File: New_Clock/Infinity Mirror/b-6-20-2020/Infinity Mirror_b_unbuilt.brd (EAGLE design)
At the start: 81 x 26 mm, 19 parts, among them IC1 MSGEQ7P, J1 Vsupply, J2 AUDIO_POTS, J3 LED, U1 DS1307, Y1 32.768kHz

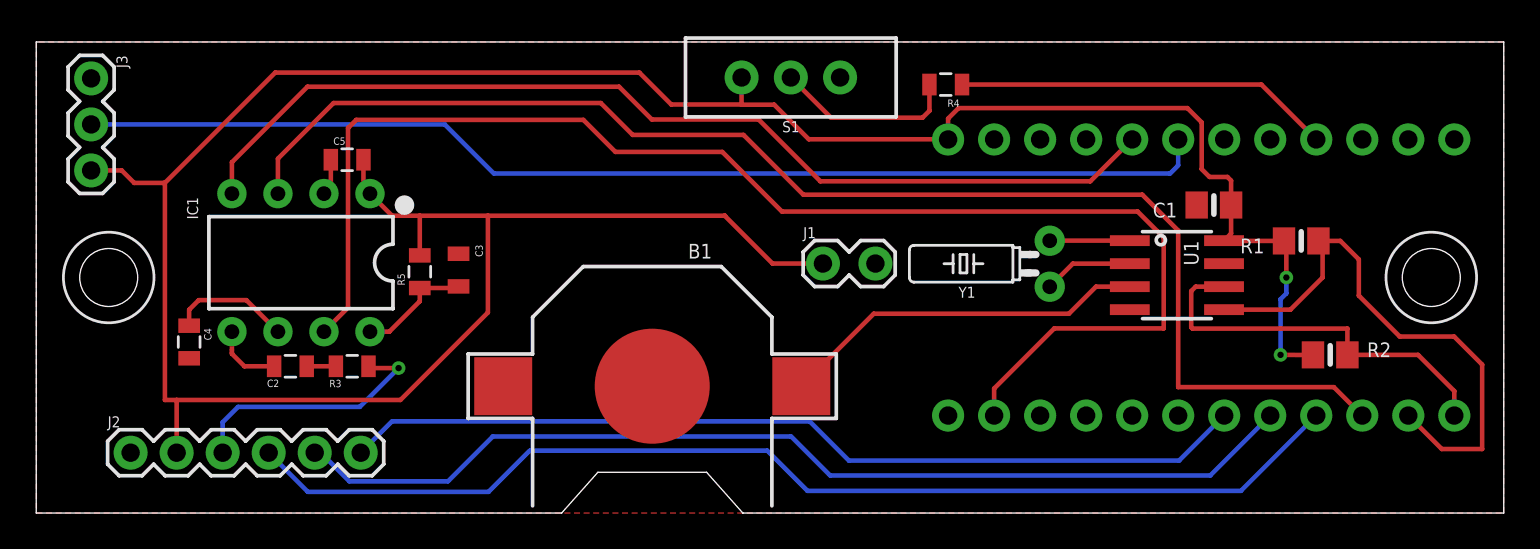
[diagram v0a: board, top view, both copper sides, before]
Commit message: created rec v with a larger board with integrated 8 throw switches. found 3D models and ported circuit box for editing in Fusion. NOTE: THIS CAD IS NOT EXACTLY THE SAME AS THE REAL CLOCK
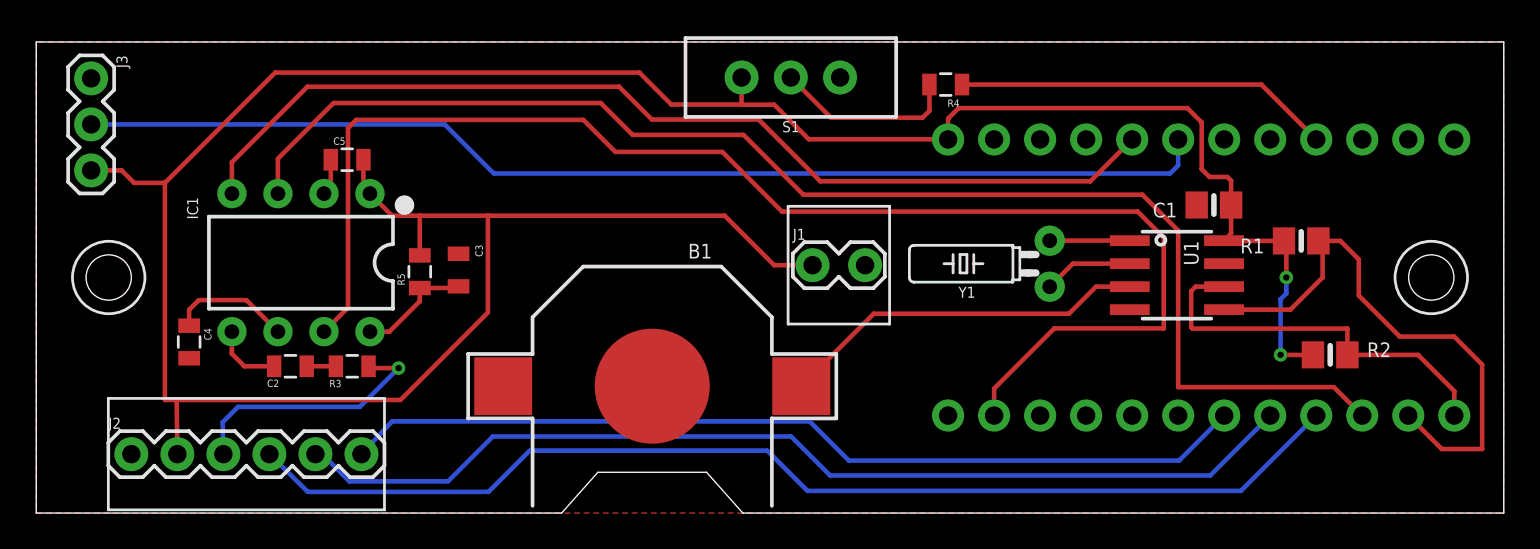
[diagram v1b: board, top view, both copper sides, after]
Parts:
- moved J1 0.58 mm to (43.0, 13.7)
- moved J2 0.09 mm to (5.25, 3.25)
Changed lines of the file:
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@@
 <wire x1="81" y1="26" x2="0" y2="26" width="0" layer="20"/>
 <wire x1="0" y1="26" x2="0" y2="0" width="0" layer="20"/>
-<hole x="77" y="13" drill="3.2"/>
-<circle x="77" y="13" radius="2.5" width="0.1524" layer="21"/>
-<hole x="4" y="13" drill="3.2"/>
-<circle x="4" y="13" radius="2.5" width="0.1524" layer="21"/>
+<hole x="77" y="13" drill="2.5"/>
+<circle x="77" y="13" radius="2" width="0.1524" layer="21"/>
+<hole x="4" y="13" drill="2.5"/>
+<circle x="4" y="13" radius="2" width="0.1524" layer="21"/>
 <wire x1="0" y1="0" x2="29" y2="0" width="0" layer="20"/>
 <wire x1="29" y1="0" x2="31" y2="2.25" width="0" layer="20"/>
@@
 <wire x1="37" y1="2.25" x2="39" y2="0" width="0" layer="20"/>
 <wire x1="39" y1="0" x2="81" y2="0" width="0" layer="20"/>
+<wire x1="3.98" y1="0.175" x2="3.98" y2="6.325" width="0.1524" layer="21"/>
+<wire x1="3.98" y1="6.325" x2="19.22" y2="6.325" width="0.1524" layer="21"/>
+<wire x1="19.22" y1="6.325" x2="19.22" y2="0.175" width="0.1524" layer="21"/>
+<wire x1="19.22" y1="0.175" x2="3.98" y2="0.175" width="0.1524" layer="21"/>
 </plain>
 <attributes>
@@
 </autorouter>
 <elements>
-<element name="J1" library="RC1a_Main_2-20-2018_m" package="SPARKFUN-CONNECTORS_1X02_LOCK" value="Vsupply" x="43.6" y="13.77" smashed="yes">
-<attribute name="NAME" x="42.33" y="15.167" size="0.6096" layer="25" font="vector" ratio="20"/>
-<attribute name="VALUE" x="42.33" y="11.738" size="0.6096" layer="27" font="vector" ratio="20"/>
+<element name="J1" library="RC1a_Main_2-20-2018_m" package="SPARKFUN-CONNECTORS_1X02_LOCK" value="Vsupply" x="43.03" y="13.68" smashed="yes">
+<attribute name="NAME" x="41.76" y="15.077" size="0.6096" layer="25" font="vector" ratio="20"/>
+<attribute name="VALUE" x="41.76" y="11.648" size="0.6096" layer="27" font="vector" ratio="20"/>
 </element>
 <element name="R2" library="microbuilder" package="0805-NO" value="10K" x="71.42" y="8.73" smashed="yes">
@@
 <attribute name="VALUE" x="13.724" y="6.953" size="0.4064" layer="27"/>
 </element>
-<element name="J2" library="SparkFun-Connectors" library_urn="urn:adsk.eagle:library:513" package="1X06" package3d_urn="urn:adsk.eagle:package:38009/1" value="AUDIO_POTS" x="5.21" y="3.33" smashed="yes">
-<attribute name="NAME" x="3.94" y="4.727" size="0.6096" layer="25" font="vector" ratio="20"/>
-<attribute name="PROD_ID" value="CONN-08437" x="5.21" y="3.33" size="1.778" layer="27" display="off"/>
-<attribute name="VALUE" x="3.94" y="1.298" size="0.6096" layer="27" font="vector" ratio="20"/>
+<element name="J2" library="SparkFun-Connectors" library_urn="urn:adsk.eagle:library:513" package="1X06" package3d_urn="urn:adsk.eagle:package:38009/1" value="AUDIO_POTS" x="5.25" y="3.25" smashed="yes">
+<attribute name="NAME" x="3.98" y="4.647" size="0.6096" layer="25" font="vector" ratio="20"/>
+<attribute name="PROD_ID" value="CONN-08437" x="5.25" y="3.25" size="1.778" layer="27" display="off"/>
+<attribute name="VALUE" x="3.98" y="1.218" size="0.6096" layer="27" font="vector" ratio="20"/>
 </element>
 <element name="R5" library="RC1a_Main_2-20-2018_m" package="SPARKFUN-PASSIVES_0805" value="200k" x="21.17" y="13.32" smashed="yes" rot="R90">
@@
 <contactref element="U$1" pad="TG"/>
 <contactref element="S1" pad="3"/>
-<wire x1="3.0378" y1="23.9978" x2="3.03" y2="23.99" width="0.1524" layer="1"/>
 <contactref element="IC1" pad="2"/>
 <polygon width="0.127" layer="1">
@@
 <contactref element="J3" pad="3"/>
 <wire x1="7.1022" y1="18.14" x2="7.1022" y2="6.24" width="0.254" layer="1"/>
-<wire x1="7.75" y1="6.24" x2="7.75" y2="3.33" width="0.254" layer="1"/>
+<wire x1="7.75" y1="6.24" x2="7.79" y2="3.25" width="0.254" layer="1"/>
 <wire x1="64.3276" y1="21.56" x2="64.3276" y2="18.98" width="0.254" layer="1"/>
 <wire x1="64.3276" y1="18.98" x2="64.7576" y2="18.55" width="0.254" layer="1"/>
@@
 <contactref element="IC1" pad="1"/>
 <contactref element="C5" pad="2"/>
-<wire x1="18.06" y1="19.5" x2="18.06" y2="17.99" width="0.254" layer="1"/>
+<wire x1="18.06" y1="17.99" x2="18.06" y2="19.5" width="0.254" layer="1"/>
 <wire x1="18.42" y1="17.63" x2="19.64" y2="16.41" width="0.254" layer="1"/>
 <wire x1="24.93" y1="11.0667125" x2="20.1032875" y2="6.24" width="0.254" layer="1"/>
 <wire x1="24.93" y1="16.41" x2="38" y2="16.41" width="0.254" layer="1"/>
-<wire x1="38" y1="16.41" x2="38.02" y2="16.41" width="0.254" layer="1"/>
 <wire x1="7.0222" y1="18.22" x2="7.1022" y2="18.14" width="0.1524" layer="1"/>
 <wire x1="7.1022" y1="6.24" x2="7.75" y2="6.24" width="0.254" layer="1"/>
@@
 <wire x1="65.75" y1="18.55" x2="65.95" y2="18.35" width="0.254" layer="1"/>
 <wire x1="65.95" y1="18.35" x2="65.95" y2="17" width="0.254" layer="1"/>
-<wire x1="38" y1="16.41" x2="40.64" y2="13.77" width="0.254" layer="1"/>
-<wire x1="40.64" y1="13.77" x2="43.4222" y2="13.77" width="0.254" layer="1"/>
+<wire x1="38" y1="16.41" x2="40.73" y2="13.68" width="0.254" layer="1"/>
+<wire x1="40.73" y1="13.68" x2="42.8522" y2="13.68" width="0.254" layer="1"/>
 <wire x1="13.19" y1="24.31" x2="33.29" y2="24.31" width="0.254" layer="1"/>
 <wire x1="35.0522" y1="22.5478" x2="38.9322" y2="22.5478" width="0.254" layer="1"/>
 <wire x1="33.29" y1="24.31" x2="35.0522" y2="22.5478" width="0.254" layer="1"/>
-<wire x1="18.42" y1="17.63" x2="18.06" y2="17.99" width="0" layer="19" extent="1-1"/>
+<wire x1="18.42" y1="17.63" x2="18.06" y2="17.99" width="0.254" layer="1"/>
 </signal>
 <signal name="SDA">
@@
 <contactref element="R3" pad="2"/>
 <contactref element="J2" pad="3"/>
-<wire x1="20" y1="8" x2="19.96" y2="8" width="0.254" layer="16"/>
 <via x="20" y="8" extent="1-16" drill="0.35"/>
 <wire x1="20" y1="8" x2="18.55" y2="8" width="0.254" layer="1"/>
 <wire x1="18.55" y1="8" x2="18.34" y2="8.1" width="0.254" layer="1"/>
 <wire x1="11.14" y1="5.86" x2="10.29" y2="5.01" width="0.254" layer="16"/>
-<wire x1="10.29" y1="3.33" x2="10.29" y2="5.01" width="0.254" layer="16"/>
-<wire x1="19.98" y1="7.98" x2="20" y2="8" width="0.254" layer="16"/>
+<wire x1="10.33" y1="3.25" x2="10.29" y2="5.01" width="0.254" layer="16"/>
 <wire x1="11.14" y1="5.86" x2="17.86" y2="5.86" width="0.254" layer="16"/>
 <wire x1="17.86" y1="5.86" x2="20" y2="8" width="0.254" layer="16"/>
@@
 <contactref element="J2" pad="6"/>
 <wire x1="42.69" y1="5.06" x2="19.64" y2="5.06" width="0.254" layer="16"/>
-<wire x1="17.91" y1="3.33" x2="19.64" y2="5.06" width="0.254" layer="16"/>
+<wire x1="17.95" y1="3.25" x2="19.64" y2="5.06" width="0.254" layer="16"/>
 <wire x1="42.69" y1="5.06" x2="44.8578" y2="2.8922" width="0.254" layer="16"/>
 <wire x1="63.0822" y1="2.8922" x2="65.57" y2="5.38" width="0.254" layer="16"/>
@@
 <wire x1="25.19756875" y1="4.2252" x2="41.66374375" y2="4.2252" width="0.254" layer="16"/>
 <wire x1="17.28603125" y1="1.7516" x2="15.70763125" y2="3.33" width="0.254" layer="16"/>
-<wire x1="15.37" y1="3.33" x2="15.70763125" y2="3.33" width="0.254" layer="16"/>
+<wire x1="15.41" y1="3.25" x2="15.70763125" y2="3.33" width="0.254" layer="16"/>
 <wire x1="22.72396875" y1="1.7516" x2="25.19756875" y2="4.2252" width="0.254" layer="16"/>
 <wire x1="41.66374375" y1="4.2252" x2="43.81674375" y2="2.0722" width="0.254" layer="16"/>
@@
 <contactref element="U$1" pad="TA2"/>
 <contactref element="J2" pad="4"/>
-<wire x1="12.83" y1="3.33" x2="14.99" y2="1.17" width="0.254" layer="16"/>
+<wire x1="12.87" y1="3.25" x2="14.99" y2="1.17" width="0.254" layer="16"/>
 <wire x1="14.99" y1="1.17" x2="24.97" y2="1.17" width="0.254" layer="16"/>
 <wire x1="27.24" y1="3.44" x2="40.35" y2="3.44" width="0.254" layer="16"/>
@@
 <contactref element="R3" pad="1"/>
 <contactref element="C2" pad="2"/>
-<wire x1="16.505" y1="7.83" x2="16.54" y2="8.1" width="0.254" layer="1"/>
 <wire x1="14.93" y1="8.1" x2="16.54" y2="8.1" width="0.254" layer="1"/>
 </signal>
@@
 <mfgpreviewcolor name="substratecolor" color="0xFF786E46"/>
 </mfgpreviewcolors>
+<errors>
+</errors>
 </board>
 </drawing>
